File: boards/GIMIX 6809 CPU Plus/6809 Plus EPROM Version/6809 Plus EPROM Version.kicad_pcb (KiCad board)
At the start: 2 copper layers, 248.9 x 139.7 mm, 164 parts, among them P1 SS-50 Bus, Q1 BC337, Q2 BC337, Q3 BC337, SW1 OPTION, SW2 CONFIG, U1 MM58167, U10 74LS04, U11 74LS161, U12 74LS161, U13 74LS123, U14 74LS74, U15 74LS00, U16 74LS32, U17 74LS136, U18 74LS20, U19 74LS32, U2 MC6840, U20 74LS12, U21 AM93L422, U22 AM93L422, U23 74LS174, U24 74LS157, U25 74LS20, U26 74LS04, U27 74LS02, U28 LM7812_TO220, U29 LM7805_TO220, U3 9511, U30 LM7805_TO220, U31 LM7905_TO220, U32 74LS30, U33 74LS240, U34 74LS368, U35 74LS136, U36 27C512, U37 DS8T28N, U38 DS8T28N, U39 74S189, U4 27C32, U40 74S189, U41 DS8T28N, U42 DS8T28N, U43 74LS174, U44 DS8T28N, U45 DS8T28N, U46 74LS30, U47 MC6809, U48 74LS244, U49 74LS640, U5 27C32, U50 74LS640, U51 74LS00, U52 74LS00, U53 74LS74, U54 74LS04, U6 27C32, U7 27C512, U8 2114, U9 2114, Y1 32k768, Y2 16M, Y3 12M

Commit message: CPU++ added
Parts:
- added BT1: Battery, Connector_PinHeader_2.54mm:PinHeader_1x02_P2.54mm_Vertical, F.Cu at (192.5, 22.4)
- C1: footprint Capacitor_THT:CP_Radial_D8.0mm_P3.50mm -> my_own:C_Trim_3pin
- moved C1 8.13 mm to (26.9, 22.6)
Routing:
- net GND: track 1170.1 -> 1229.3 mm, vias 47 -> 53
- net Net-(U1-OSC_In): track 54.6 -> 70.1 mm
- net Net-(C2-Pad1): track 35.7 -> 30.7 mm, vias 0 -> 1
- net Net-(BT1-+): track 2.54 -> 7.21 mm
- net -5V: track 250.0 -> 247.2 mm
- net +5B: track 318.1 -> 315.7 mm
- net +5A: track 803.5 -> 805.7 mm
- net +12V: track 253.3 -> 251.6 mm
- net Net-(U1-~{WR}): track 65.7 -> 64.4 mm
- net /~{RDY}: track 158.5 -> 157.8 mm
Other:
- board text added: "GIMIX 6809 CPU+ Remake by 100% Offner 2026 v1.0"
- board text removed: "GIMIX 6809 CPU+ Remake by 100% Offner 2025 v1.0"

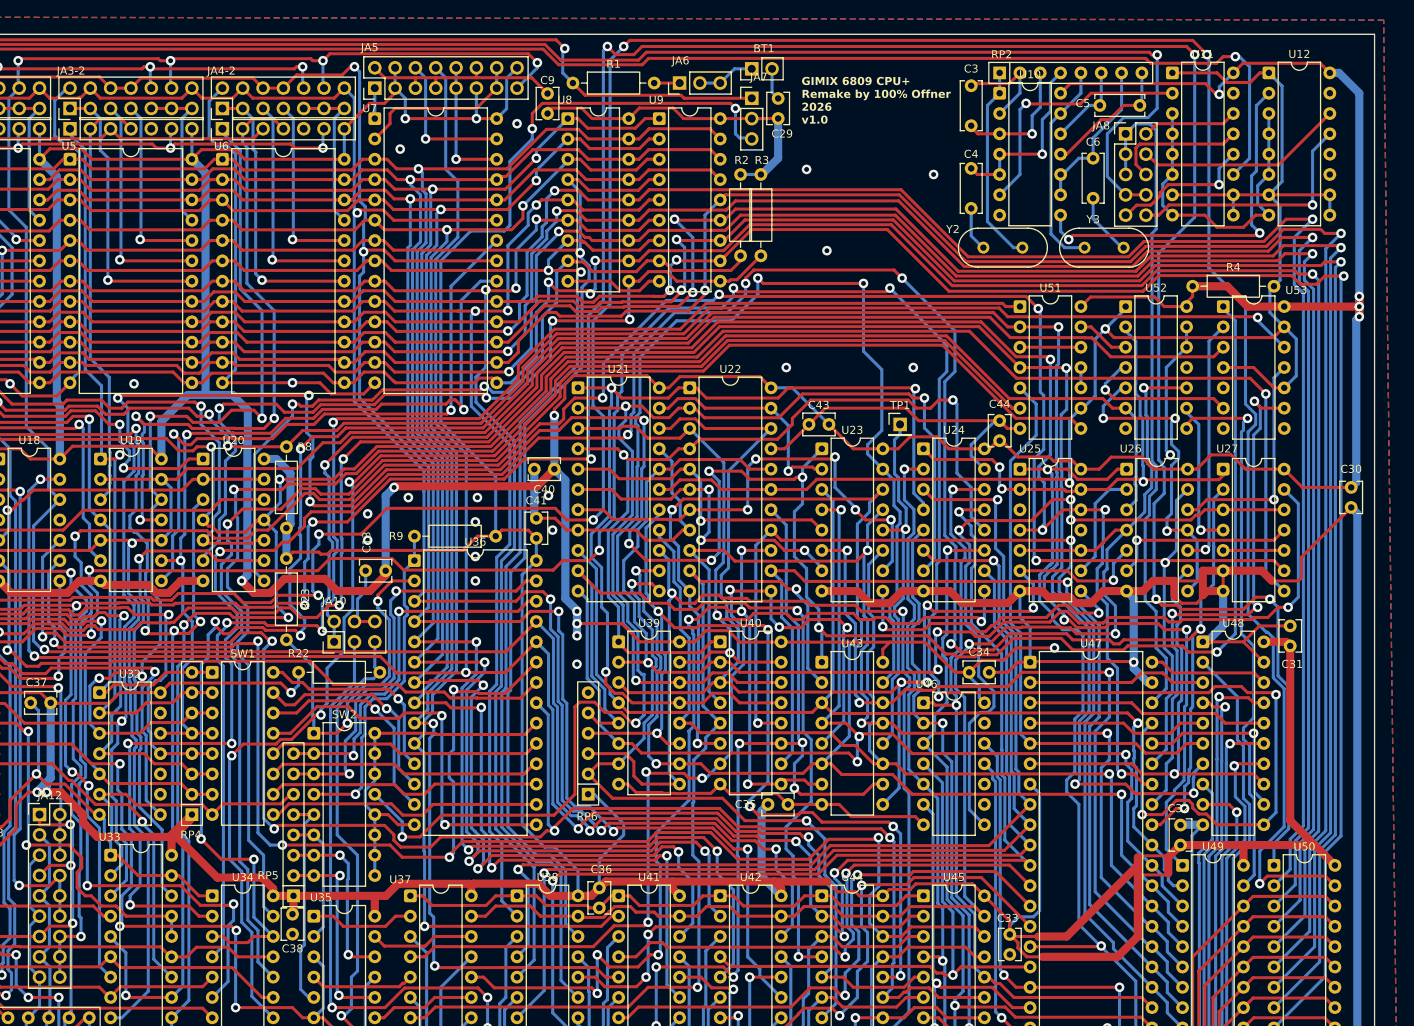
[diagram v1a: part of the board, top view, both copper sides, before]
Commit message: CPU Plus Battery added
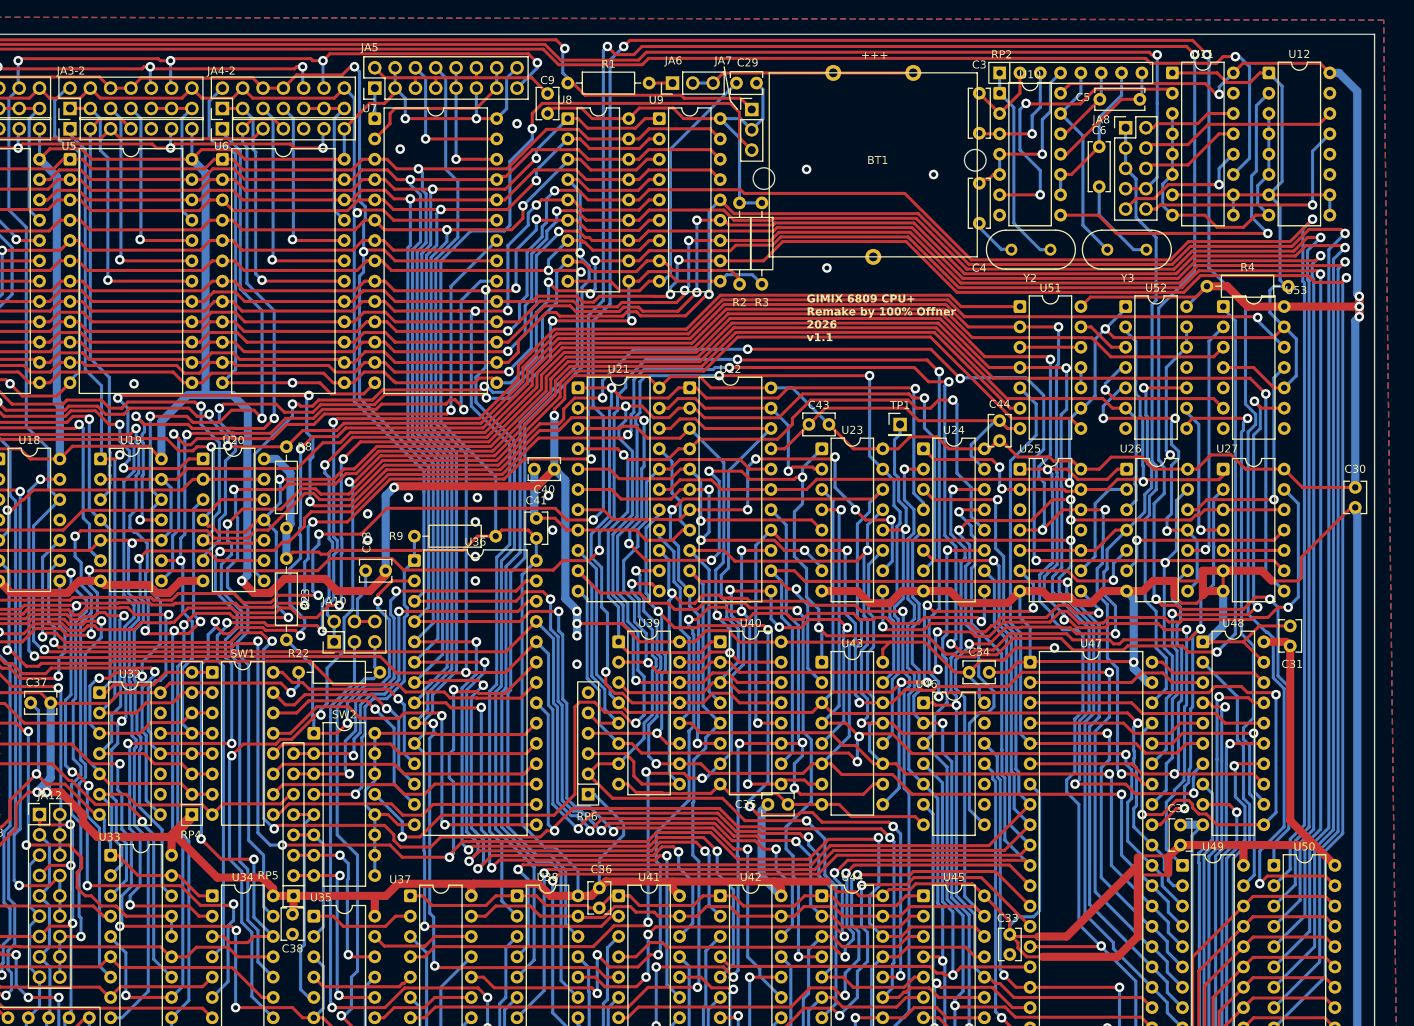
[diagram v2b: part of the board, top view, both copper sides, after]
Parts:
- added H1: MountingHole, MountingHole:MountingHole_2.7mm, F.Cu at (194.1, 36.1)
- added H2: MountingHole, MountingHole:MountingHole_2.7mm, F.Cu at (220.5, 33.8)
- BT1: footprint Connector_PinHeader_2.54mm:PinHeader_1x02_P2.54mm_Vertical -> my_own:Varta_3V200HSKSPCBD
- moved BT1 19.4 mm to (207.7, 34.4), turned to 180 degrees
- moved C29 5.19 mm to (193.1, 24.1), turned to 180 degrees
- moved R2 3.56 mm to (191.0, 39.1)
- moved R3 3.56 mm to (193.8, 39.1)
- moved Y2 3.51 mm to (229.9, 45.0)
- moved Y3 2.86 mm to (237.0, 45.0)
- moved C4 2.12 mm to (221.0, 41.7)
- moved R4 1.78 mm to (249.4, 49.5)
- moved C6 1.63 mm to (236.0, 37.1)
- moved JA7 1.40 mm to (192.5, 27.4)
- moved C3 1.38 mm to (221.0, 25.4)
- moved JA6 0.89 mm to (182.6, 24.1)
- moved C5 0.76 mm to (236.0, 26.2)
- moved JA8 0.76 mm to (239.3, 29.7)
- moved R1 0.64 mm to (169.5, 24.1)
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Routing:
- net GND: track 1229.3 -> 1254.7 mm, vias 53 -> 51
- net /FPLA_CTRL: track 187.5 -> 166.4 mm
- net Net-(BT1-+): track 7.21 -> 27.5 mm
- net /CR/~{W}: track 309.6 -> 291.6 mm
- net /CPU/~{CRESET}: track 321.0 -> 307.3 mm
- net /CQ: track 317.7 -> 305.0 mm
- net /CPU/CPUCLK: track 84.2 -> 76.3 mm
- net Net-(JA7-Pin_2): track 41.6 -> 49.5 mm
- net Net-(U11-CP): track 31.7 -> 37.2 mm, vias 1 -> 2
- net /Clock/CLK9511: track 203.1 -> 197.6 mm
- net /Clock/4M: track 16.7 -> 12.7 mm
- net Net-(RP2A-R1.2): track 13.0 -> 9.72 mm
- net Net-(C6-Pad1): track 8.03 -> 11.2 mm
- net /ID5: track 389.6 -> 386.6 mm
- net +5C: track 883.8 -> 886.0 mm
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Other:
- board text added: "GIMIX 6809 CPU+ Remake by 100% Offner 2026 v1.1"
- board text removed: "GIMIX 6809 CPU+ Remake by 100% Offner 2026 v1.0"
